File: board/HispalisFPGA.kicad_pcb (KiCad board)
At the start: 4 copper layers, 90 x 102.1 mm, 126 parts, among them Q1 DMG1012T, Q2 DMG1012T, Q3 DMG1012T, Q4 DMG1012T, SW1 SW_DIP_x08

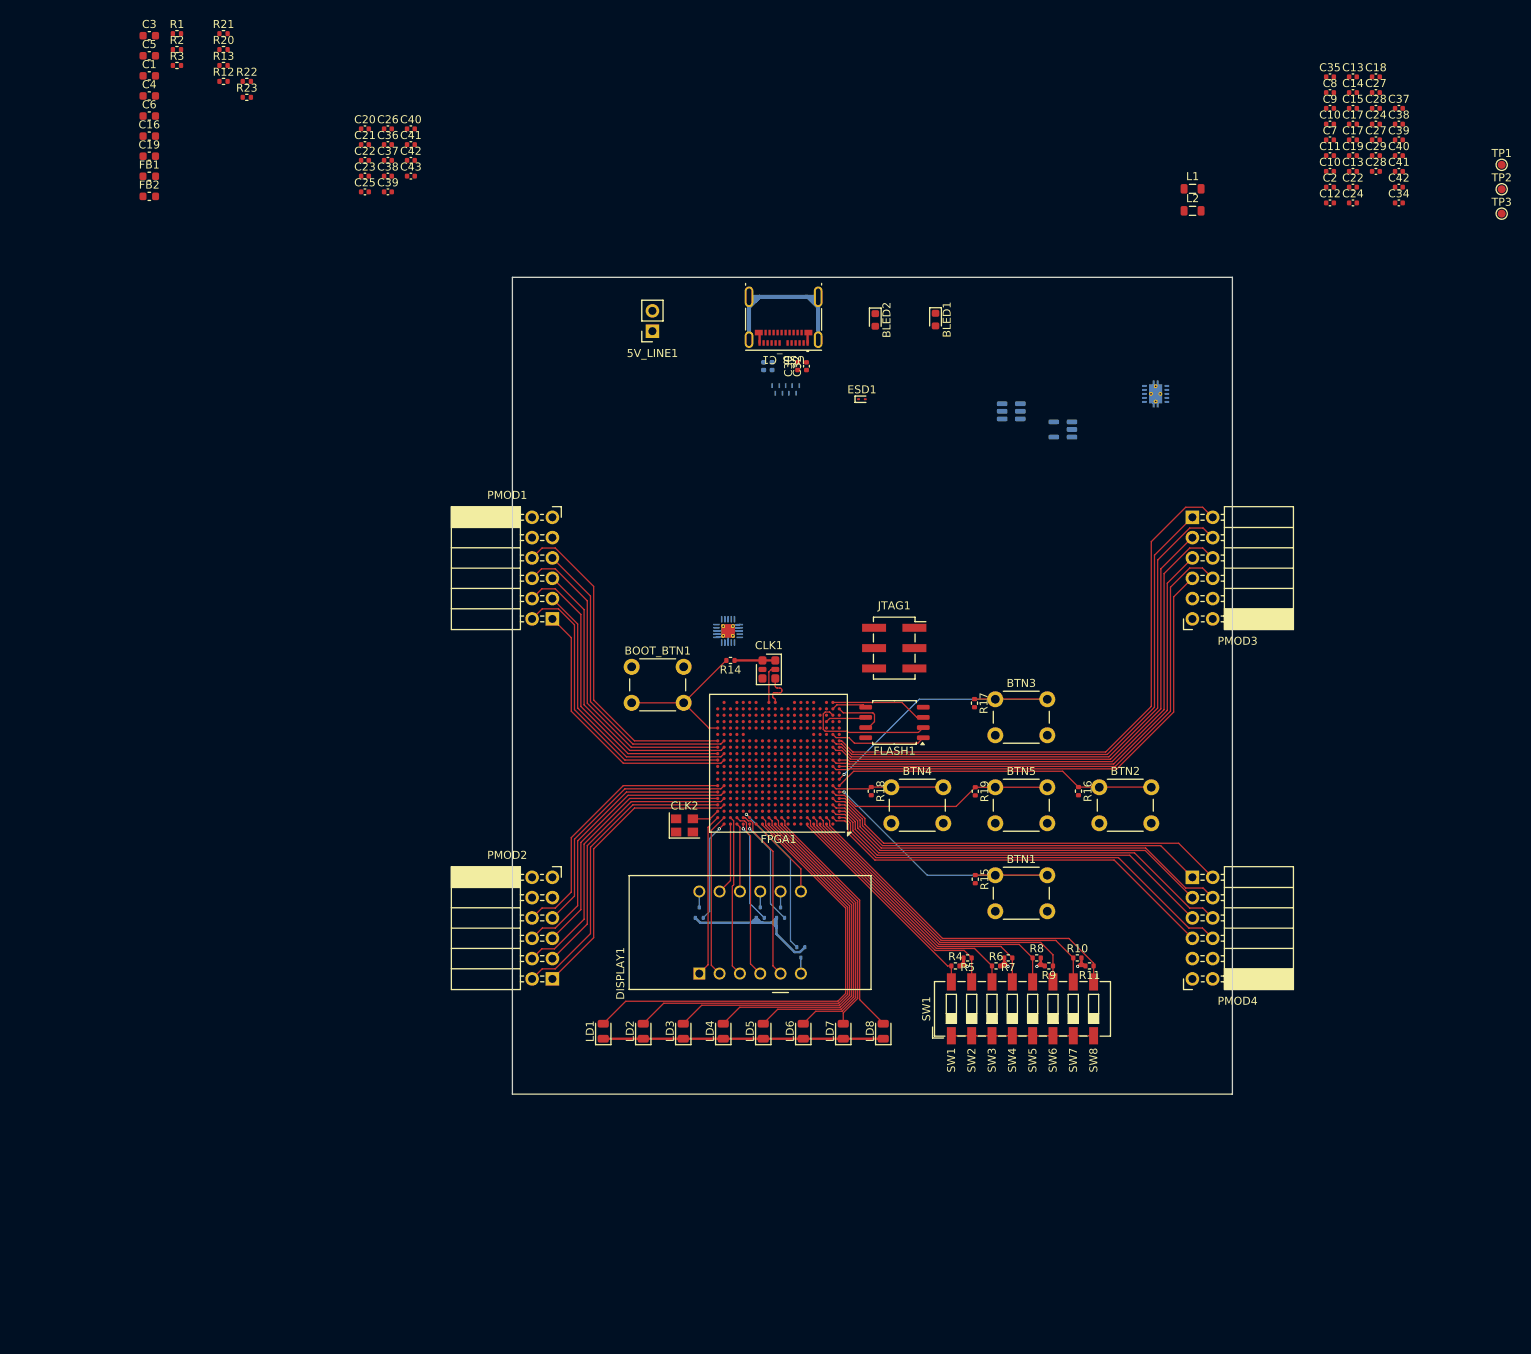
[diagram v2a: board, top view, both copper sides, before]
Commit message: Change USB 3.1 for USB 2.0 Type-C and use JTAG and serial USB controller
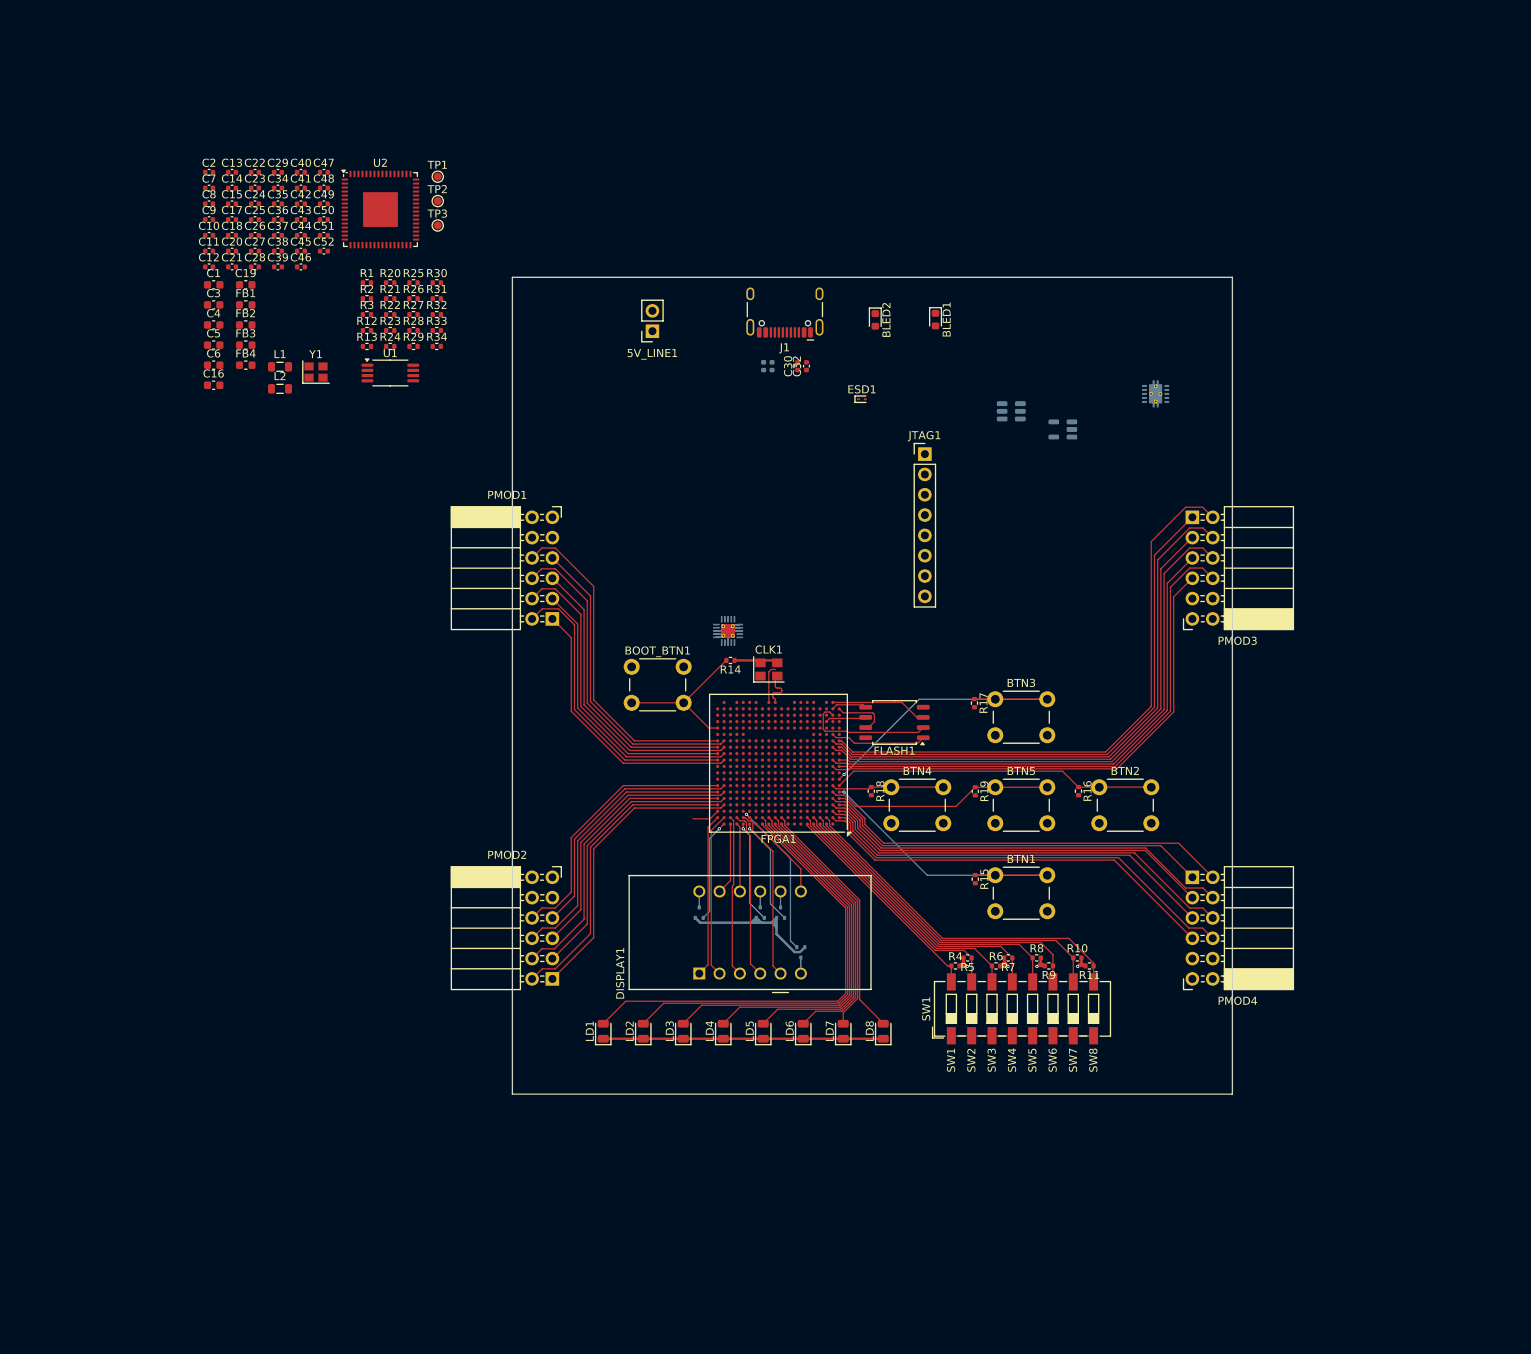
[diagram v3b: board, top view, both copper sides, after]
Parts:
- removed the C10 at (216.6, 31.7)
- removed the C10 at (216.6, 37.6)
- removed the C13 at (219.5, 37.6)
- removed the C13 at (219.5, 25.8)
- removed the C17 at (219.5, 33.7)
- removed the C17 at (219.5, 31.7)
- removed the C19 at (69.0, 35.7)
- removed the C19 at (219.5, 35.6)
- removed the C22 at (219.5, 39.6)
- removed the C22 at (96.0, 36.2)
- removed the C24 at (222.4, 31.7)
- removed the C24 at (219.5, 41.6)
- removed the C27 at (222.4, 33.7)
- removed the C27 at (222.4, 27.8)
- removed the C28 at (222.4, 37.6)
- removed the C28 at (222.4, 29.7)
- removed the C37 at (225.2, 29.7)
- removed the C37 at (98.9, 36.2)
- removed the C38 at (225.2, 31.7)
- removed the C38 at (98.9, 38.2)
- removed the C39 at (98.9, 40.2)
- removed the C39 at (225.2, 33.7)
- removed the C40 at (101.8, 32.3)
- removed the C40 at (225.2, 35.6)
- removed the C41 at (101.8, 34.3)
- removed the C41 at (225.2, 37.6)
- removed the C42 at (101.8, 36.2)
- removed the C42 at (225.2, 39.6)
- removed CLK2: ASEDV-16.000MHZ-LR-T, Oscillator:Oscillator_SMD_Abracon_ASE-4Pin_3.2x2.5mm
- removed ESD3: DT1240A-08LP3810, Package_DFN_QFN:UDFN-9_1.0x3.8mm_P0.5mm
- removed USB_C1: MOLEX-105450-0101, Connector_USB:USB_C_Receptacle_Molex_105450-0101
- added C10: 100nF, Capacitor_SMD:C_0402_1005Metric, F.Cu at (76.5, 45.6)
- added C13: 100nF, Capacitor_SMD:C_0402_1005Metric, F.Cu at (79.4, 37.7)
- added C17: 10nF, Capacitor_SMD:C_0402_1005Metric, F.Cu at (79.4, 43.6)
- added C19: 22uF, Capacitor_SMD:C_0603_1608Metric, F.Cu at (81.1, 51.8)
- added C22: 100nF, Capacitor_SMD:C_0402_1005Metric, F.Cu at (82.3, 37.7)
- added C24: 1uF, Capacitor_SMD:C_0402_1005Metric, F.Cu at (82.3, 41.7)
- added C27: 100nF, Capacitor_SMD:C_0402_1005Metric, F.Cu at (82.3, 47.6)
- added C28: 100nF, Capacitor_SMD:C_0402_1005Metric, F.Cu at (82.3, 49.6)
- added C37: 100nF, Capacitor_SMD:C_0402_1005Metric, F.Cu at (85.1, 45.6)
- added C38: 3.3uF, Capacitor_SMD:C_0402_1005Metric, F.Cu at (85.1, 47.6)
- added C39: 100nF, Capacitor_SMD:C_0402_1005Metric, F.Cu at (85.1, 49.6)
- added C40: 100nF, Capacitor_SMD:C_0402_1005Metric, F.Cu at (88.0, 37.7)
- added C41: 100nF, Capacitor_SMD:C_0402_1005Metric, F.Cu at (88.0, 39.7)
- added C42: 100nF, Capacitor_SMD:C_0402_1005Metric, F.Cu at (88.0, 41.7)
- added C44: 100nF, Capacitor_SMD:C_0402_1005Metric, F.Cu at (88.0, 45.6)
- added C45: 100nF, Capacitor_SMD:C_0402_1005Metric, F.Cu at (88.0, 47.6)
- added C46: 10nF, Capacitor_SMD:C_0402_1005Metric, F.Cu at (88.0, 49.6)
- added C47: 100nF, Capacitor_SMD:C_0402_1005Metric, F.Cu at (90.9, 37.7)
- added C48: 10nF, Capacitor_SMD:C_0402_1005Metric, F.Cu at (90.9, 39.7)
- added C49: 100nF, Capacitor_SMD:C_0402_1005Metric, F.Cu at (90.9, 41.7)
- added C50: 10nF, Capacitor_SMD:C_0402_1005Metric, F.Cu at (90.9, 43.6)
- added C51: 100nF, Capacitor_SMD:C_0402_1005Metric, F.Cu at (90.9, 45.6)
- added C52: 10nF, Capacitor_SMD:C_0402_1005Metric, F.Cu at (90.9, 47.6)
- added FB3: 600R@100MHz, Inductor_SMD:L_0603_1608Metric, F.Cu at (81.1, 59.3)
- added FB4: 600R@100MHz, Inductor_SMD:L_0603_1608Metric, F.Cu at (81.1, 61.8)
- added J1: HC-TYPE-C-16P-01A, Connector_USB:USB_C_Receptacle_HCTL_HC-TYPE-C-16P-01A, F.Cu at (148.5, 54.0)
- added R24: 4.7K, Resistor_SMD:R_0402_1005Metric, F.Cu at (99.2, 59.5)
- added R25: 2.2K, Resistor_SMD:R_0402_1005Metric, F.Cu at (102.1, 51.5)
- added R26: 4.7K, Resistor_SMD:R_0402_1005Metric, F.Cu at (102.1, 53.5)
- added R27: 10K, Resistor_SMD:R_0402_1005Metric, F.Cu at (102.1, 55.5)
- added R28: 2K, Resistor_SMD:R_0402_1005Metric, F.Cu at (102.1, 57.5)
- added R29: 10K, Resistor_SMD:R_0402_1005Metric, F.Cu at (102.1, 59.5)
- added R30: 12K, Resistor_SMD:R_0402_1005Metric, F.Cu at (105.0, 51.5)
- added R31: 10K, Resistor_SMD:R_0402_1005Metric, F.Cu at (105.0, 53.5)
- added R32: 1K, Resistor_SMD:R_0402_1005Metric, F.Cu at (105.0, 55.5)
- added R33: 5.1K, Resistor_SMD:R_0402_1005Metric, F.Cu at (105.0, 57.5)
- added R34: 5.1K, Resistor_SMD:R_0402_1005Metric, F.Cu at (105.0, 59.5)
- added U1: 93LC46B, Package_SO:TSSOP-8_4.4x3mm_P0.65mm, F.Cu at (99.2, 62.8)
- added U2: FT2232HQ, Package_DFN_QFN:QFN-64-1EP_9x9mm_P0.5mm_EP4.35x4.35mm, F.Cu at (98.0, 42.4)
- added Y1: 12MHz, Crystal:Crystal_SMD_2520-4Pin_2.5x2.0mm, F.Cu at (89.9, 62.7)
- C30, C32: value 100nF -> 4.7uF
- C33, C34: value 100nF -> 10pF
- C43: value 10nF -> 100nF
- CLK1: value SWPM201DCAIAB-200.000000 -> ASEDV-16.000MHZ-LR-T; footprint Oscillator:Oscillator_SMD_SiTime_PQFD-6L_3.2x2.5mm -> Oscillator:Oscillator_SMD_Abracon_ASE-4Pin_3.2x2.5mm
- FB1, FB2: value 100MHz -> 600R@100MHz
- JTAG1: value Conn_02x03_Odd_Even -> Conn_01x08; footprint Connector_PinSocket_2.54mm:PinSocket_2x03_P2.54mm_Vertical_SMD -> Connector_PinHeader_2.54mm:PinHeader_1x08_P2.54mm_Vertical
- R23: value 1.5K -> 4.7K
- moved C18 144.3 mm to (79.4, 45.6)
- moved C8 140.8 mm to (76.5, 41.7)
- moved C9 140.8 mm to (76.5, 43.6)
- moved C11 140.6 mm to (76.5, 47.6)
- moved C14 140.6 mm to (79.4, 39.7)
- moved C15 140.6 mm to (79.4, 41.7)
- moved C12 140.3 mm to (76.5, 49.6)
- moved C7 140.2 mm to (76.5, 39.7)
- moved C34 140.1 mm to (85.1, 39.7)
- moved C2 140.1 mm to (76.5, 37.7)
- moved C29 137.3 mm to (85.1, 37.7)
- moved TP1 133.0 mm to (105.1, 38.3)
- moved TP2 133.0 mm to (105.1, 41.3)
- moved TP3 133.0 mm to (105.1, 44.4)
- moved C35 132.5 mm to (85.1, 41.7)
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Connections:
- C29 pad 1: Net-(USB_C1-SHIELD) -> Net-(U2-VREGOUT)
- C30 pad 1: CH0_TX- -> Net-(U2-VPLL)
- C30 pad 2: Net-(USB_C1-TX1-) -> GND
- C31 pad 1: Net-(USB_C1-TX2+) -> Net-(U2-VREGOUT)
- C31 pad 2: CH1_TX+ -> GND
- C32 pad 1: CH0_TX+ -> Net-(U2-VPHY)
- C32 pad 2: Net-(USB_C1-TX1+) -> GND
- C33 pad 1: Net-(USB_C1-TX2-) -> GND
- C33 pad 2: CH1_TX- -> Net-(U2-OSCI)
- C34 pad 1: Net-(ESD2-VBIAS) -> GND
- C34 pad 2: GND -> Net-(U2-OSCO)
- C35 pad 1: +3V3 -> Net-(U2-VREGOUT)
- C36 pad 1: +3V3 -> Net-(J1-SHIELD)
- C43 pad 1: +3V3 -> +3.3V
- CLK1 pad 2: unconnected-(CLK1-NC-Pad2) -> GND
- CLK1 pad 3: GND -> CLK_16MHz
- CLK1 pad 4: Net-(CLK1-OUT+) -> +3V3
- ESD2 pad 1: Net-(ESD2-C_SBU1) -> unconnected-(ESD2-C_SBU1-Pad1)
- ESD2 pad 11: CC2 -> Net-(ESD2-CC2)
- ESD2 pad 12: CC1 -> Net-(ESD2-CC1)
- ESD2 pad 14: SBU2 -> unconnected-(ESD2-SBU2-Pad14)
- ESD2 pad 15: SBU1 -> unconnected-(ESD2-SBU1-Pad15)
- ESD2 pad 2: Net-(ESD2-C_SBU2) -> unconnected-(ESD2-C_SBU2-Pad2)
- FB1 pad 1: Net-(USB_C1-SHIELD) -> +3.3V
- FB1 pad 2: GND -> Net-(U2-VPLL)
- FB2 pad 1: +5V -> +3.3V
- FB2 pad 2: Net-(ESD1-A2) -> Net-(U2-VPHY)
- FPGA1 pad M3: USB_D- -> RXD_UART
- FPGA1 pad N3: USB_D+ -> TXD_UART
- FPGA1 pad U17: CC2 -> unconnected-(FPGA1E-PR92B-PadU17)
- FPGA1 pad U18: CC1 -> unconnected-(FPGA1E-PR92A-PadU18)
- FPGA1 pad U19: SBU2 -> unconnected-(FPGA1E-PR89C-PadU19)
- FPGA1 pad U20: SBU1 -> unconnected-(FPGA1E-PR86D-PadU20)
- FPGA1 pad W4: CH0_TX+ -> unconnected-(FPGA1J-HDTXP0_D0CH0-PadW4)
- FPGA1 pad W5: CH0_TX- -> unconnected-(FPGA1J-HDTXN0_D0CH0-PadW5)
- FPGA1 pad W8: CH1_TX+ -> unconnected-(FPGA1J-HDTXP0_D0CH1-PadW8)
- FPGA1 pad W9: CH1_TX- -> unconnected-(FPGA1J-HDTXN0_D0CH1-PadW9)
- FPGA1 pad Y11: Net-(CLK1-OUT+) -> unconnected-(FPGA1J-REFCLKP_D0-PadY11)
- FPGA1 pad Y12: Net-(CLK1-OUT-) -> unconnected-(FPGA1J-REFCLKN_D0-PadY12)
- FPGA1 pad Y5: CH0_RX+ -> unconnected-(FPGA1J-HDRXP0_D0CH0-PadY5)
- FPGA1 pad Y6: CH0_RX- -> unconnected-(FPGA1J-HDRXN0_D0CH0-PadY6)
- FPGA1 pad Y7: CH1_RX+ -> unconnected-(FPGA1J-HDRXP0_D0CH1-PadY7)
- FPGA1 pad Y8: CH1_RX- -> unconnected-(FPGA1J-HDRXN0_D0CH1-PadY8)
- JTAG1 pad 2: TCK -> TDO
- JTAG1 pad 3: GND -> TDI
- JTAG1 pad 4: TDI -> unconnected-(JTAG1-Pin_4-Pad4)
- JTAG1 pad 5: TDO -> unconnected-(JTAG1-Pin_5-Pad5)
- R22 pad 1: TCK -> +3V3
- R22 pad 2: GND -> TDO
- R23 pad 1: USB_D+ -> +3V3
- R23 pad 2: USB_CONNECT -> TDI
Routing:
- net Net-(USB_C1-SHIELD): track 25.4 -> 0.00 mm
- net unconnected-(FPGA1J-REFCLKN_D0-PadY12): track 0.00 -> 4.75 mm
- net Net-(CLK1-OUT-): track 4.75 -> 0.00 mm
- net Net-(CLK1-OUT+): track 4.70 -> 0.00 mm
- net (no net): track 0.00 -> 4.70 mm
- net GND: track 83.8 -> 81.1 mm

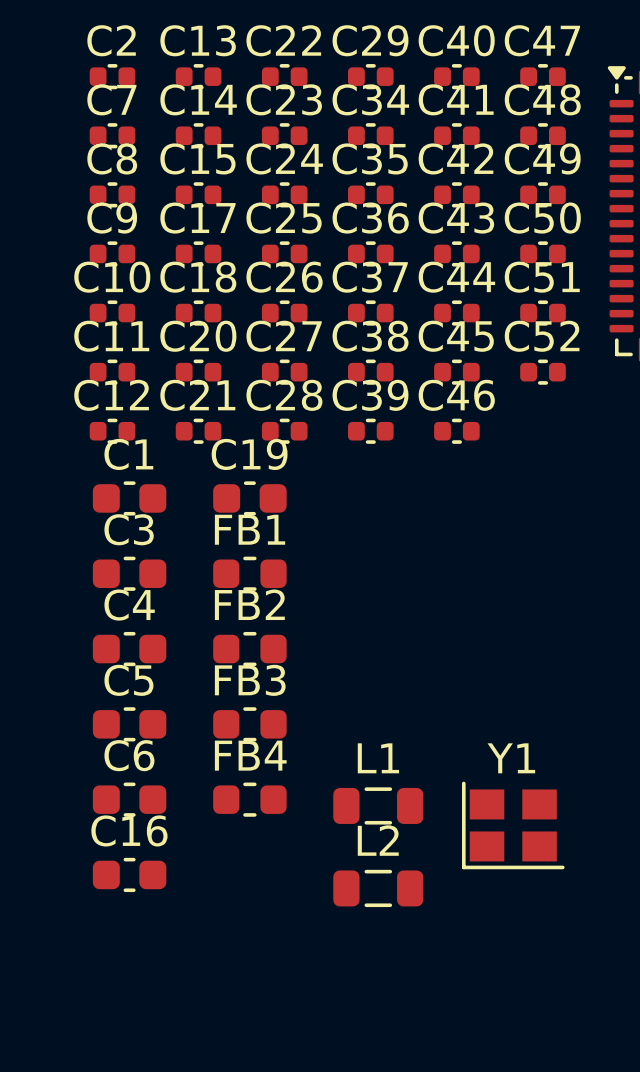
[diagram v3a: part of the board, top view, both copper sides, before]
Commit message: Subdivide schematic
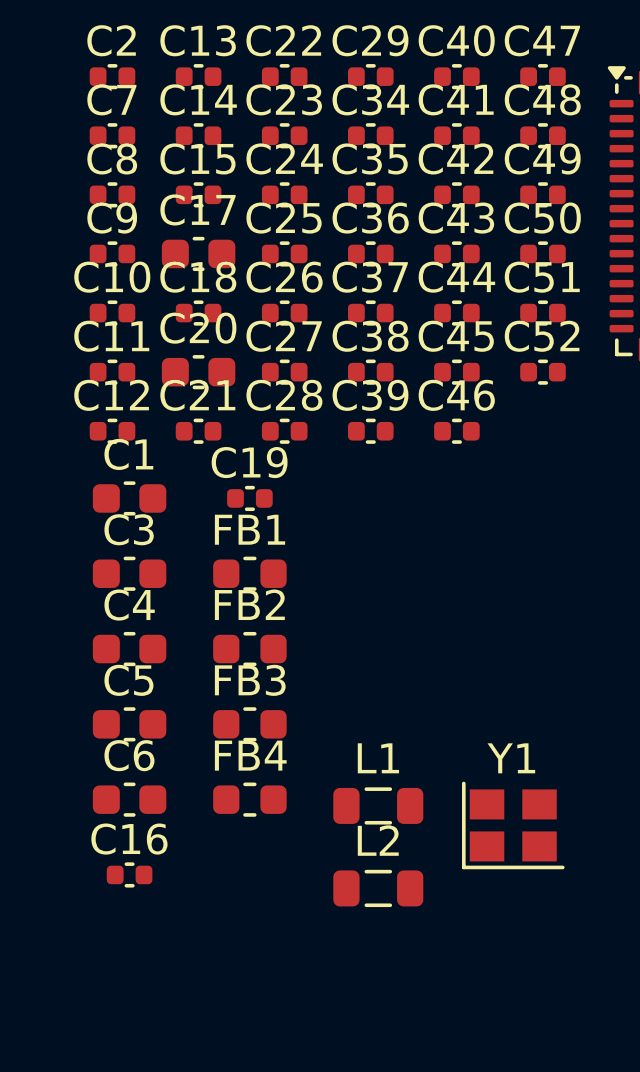
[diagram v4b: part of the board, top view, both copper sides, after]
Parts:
- C16: value 22uF -> 10nF; footprint Capacitor_SMD:C_0603_1608Metric -> Capacitor_SMD:C_0402_1005Metric
- C17: value 10nF -> 22uF; footprint Capacitor_SMD:C_0402_1005Metric -> Capacitor_SMD:C_0603_1608Metric
- C18: value 1uF -> 100nF
- C19: value 22uF -> 1uF; footprint Capacitor_SMD:C_0603_1608Metric -> Capacitor_SMD:C_0402_1005Metric
- C20: value 100nF -> 22uF; footprint Capacitor_SMD:C_0402_1005Metric -> Capacitor_SMD:C_0603_1608Metric
- C30, C32: value 4.7uF -> 100nF
- C31: value 100nF -> 4.7uF
- C33: value 10pF -> 4.7uF
- C35: value 100nF -> 10pF
- C44: value 100nF -> 10nF
- C52: value 10nF -> 100nF
- R11: value 10K -> 2K
- R12, R20, R21, R22, R23, R24, R26: value 4.7K -> 10K
- R13: value 4.7K -> 12K
- R15: value 10K -> 1K
- R25: value 2.2K -> 10K
- R28: value 2K -> 10K
- R29, R4, R5, R6: value 10K -> 4.7K
- R30: value 12K -> 4.7K
- R32: value 1K -> 4.7K
- R33, R34: value 5.1K -> 4.7K
- R7: value 10K -> 2.2K
- R8, R9: value 10K -> 5.1K
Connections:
- C18 pad 1: +5V -> +1V1
- C19 pad 1: +1V1 -> +5V
- C27 pad 1: +3V3 -> Net-(J1-SHIELD)
- C28 pad 1: +3.3V -> Net-(ESD2-VBIAS)
- C29 pad 1: Net-(U2-VREGOUT) -> +3.3V
- C30 pad 1: Net-(U2-VPLL) -> Net-(U2-VREGOUT)
- C31 pad 1: Net-(U2-VREGOUT) -> Net-(U2-VPLL)
- C32 pad 1: Net-(U2-VPHY) -> Net-(U2-VREGOUT)
- C33 pad 1: GND -> Net-(U2-VPHY)
- C33 pad 2: Net-(U2-OSCI) -> GND
- C34 pad 2: Net-(U2-OSCO) -> Net-(U2-OSCI)
- C35 pad 1: Net-(U2-VREGOUT) -> GND
- C35 pad 2: GND -> Net-(U2-OSCO)
- C36 pad 1: Net-(J1-SHIELD) -> Net-(U2-VREGOUT)
- C41 pad 1: Net-(ESD2-VBIAS) -> +3.3V
- C43 pad 1: +3.3V -> +3V3
- FB1 pad 1: +3.3V -> Net-(J1-SHIELD)
- FB1 pad 2: Net-(U2-VPLL) -> GND
- FB2 pad 1: +3.3V -> +5V
- FB2 pad 2: Net-(U2-VPHY) -> Net-(ESD1-A2)
- FB3 pad 1: Net-(J1-SHIELD) -> +3.3V
- FB3 pad 2: GND -> Net-(U2-VPLL)
- FB4 pad 1: +5V -> +3.3V
- FB4 pad 2: Net-(ESD1-A2) -> Net-(U2-VPHY)
- FPGA1 pad P5: USB_CONNECT -> unconnected-(FPGA1F-PL83D-PadP5)
- R10 pad 1: SW7 -> Net-(U1-DO)
- R10 pad 2: GND -> +3.3V
- R11 pad 1: SW8 -> Net-(U1-DO)
- R11 pad 2: GND -> Net-(U1-DI)
- R12 pad 1: Net-(FPGA1I-DONE) -> +3.3V
- R12 pad 2: Net-(BLED1-A) -> Net-(U1-SCLK)
- R13 pad 1: +3V3 -> Net-(U2-REF)
- R13 pad 2: Net-(BLED2-A) -> GND
- R14 pad 1: +3V3 -> Net-(U1-CS)
- R14 pad 2: PROGRAMN -> +3.3V
- R15 pad 1: BTN1 -> +3.3V
- R15 pad 2: GND -> Net-(U2-~{RESET})
- R16 pad 1: BTN2 -> SW1
- R17 pad 1: BTN3 -> SW2
- R18 pad 1: BTN4 -> SW3
- R19 pad 1: BTN5 -> SW4
- R20 pad 1: +3V3 -> SW5
- R20 pad 2: Net-(FPGA1I-CFG_1) -> GND
- R21 pad 1: Net-(FPGA1I-CFG_0) -> SW6
- R22 pad 1: +3V3 -> SW7
- R22 pad 2: TDO -> GND
- R23 pad 1: +3V3 -> SW8
- R23 pad 2: TDI -> GND
- R24 pad 1: +3V3 -> BTN1
- R24 pad 2: TMS -> GND
- R25 pad 1: TCK -> BTN2
- R26 pad 1: TCK -> BTN3
- R27 pad 1: Net-(U1-DO) -> BTN4
- R27 pad 2: +3.3V -> GND
- R28 pad 1: Net-(U1-DO) -> BTN5
- R28 pad 2: Net-(U1-DI) -> GND
- R29 pad 1: +3.3V -> Net-(FPGA1I-DONE)
- R29 pad 2: Net-(U1-SCLK) -> Net-(BLED1-A)
- R30 pad 1: Net-(U2-REF) -> +3V3
- R30 pad 2: GND -> Net-(BLED2-A)
- R31 pad 1: Net-(U1-CS) -> +3V3
- R31 pad 2: +3.3V -> PROGRAMN
- R32 pad 1: +3.3V -> +3V3
- R32 pad 2: Net-(U2-~{RESET}) -> Net-(FPGA1I-CFG_1)
- R33 pad 1: Net-(ESD2-CC1) -> Net-(FPGA1I-CFG_0)
- R34 pad 1: Net-(ESD2-CC2) -> TCK
- R4 pad 1: SW1 -> +3V3
- R4 pad 2: GND -> TDO
- R5 pad 1: SW2 -> +3V3
- R5 pad 2: GND -> TDI
- R6 pad 1: SW3 -> +3V3
- R6 pad 2: GND -> TMS
- R7 pad 1: SW4 -> TCK
- R8 pad 1: SW5 -> Net-(ESD2-CC1)
- R9 pad 1: SW6 -> Net-(ESD2-CC2)
